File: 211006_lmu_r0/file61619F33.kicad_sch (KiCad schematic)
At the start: 46 parts, among them J5 Conn_01x03, J6 Conn_01x03, J7 Conn_01x02, Q1 CZT5551, U3 LTC6811HG-2#PBF

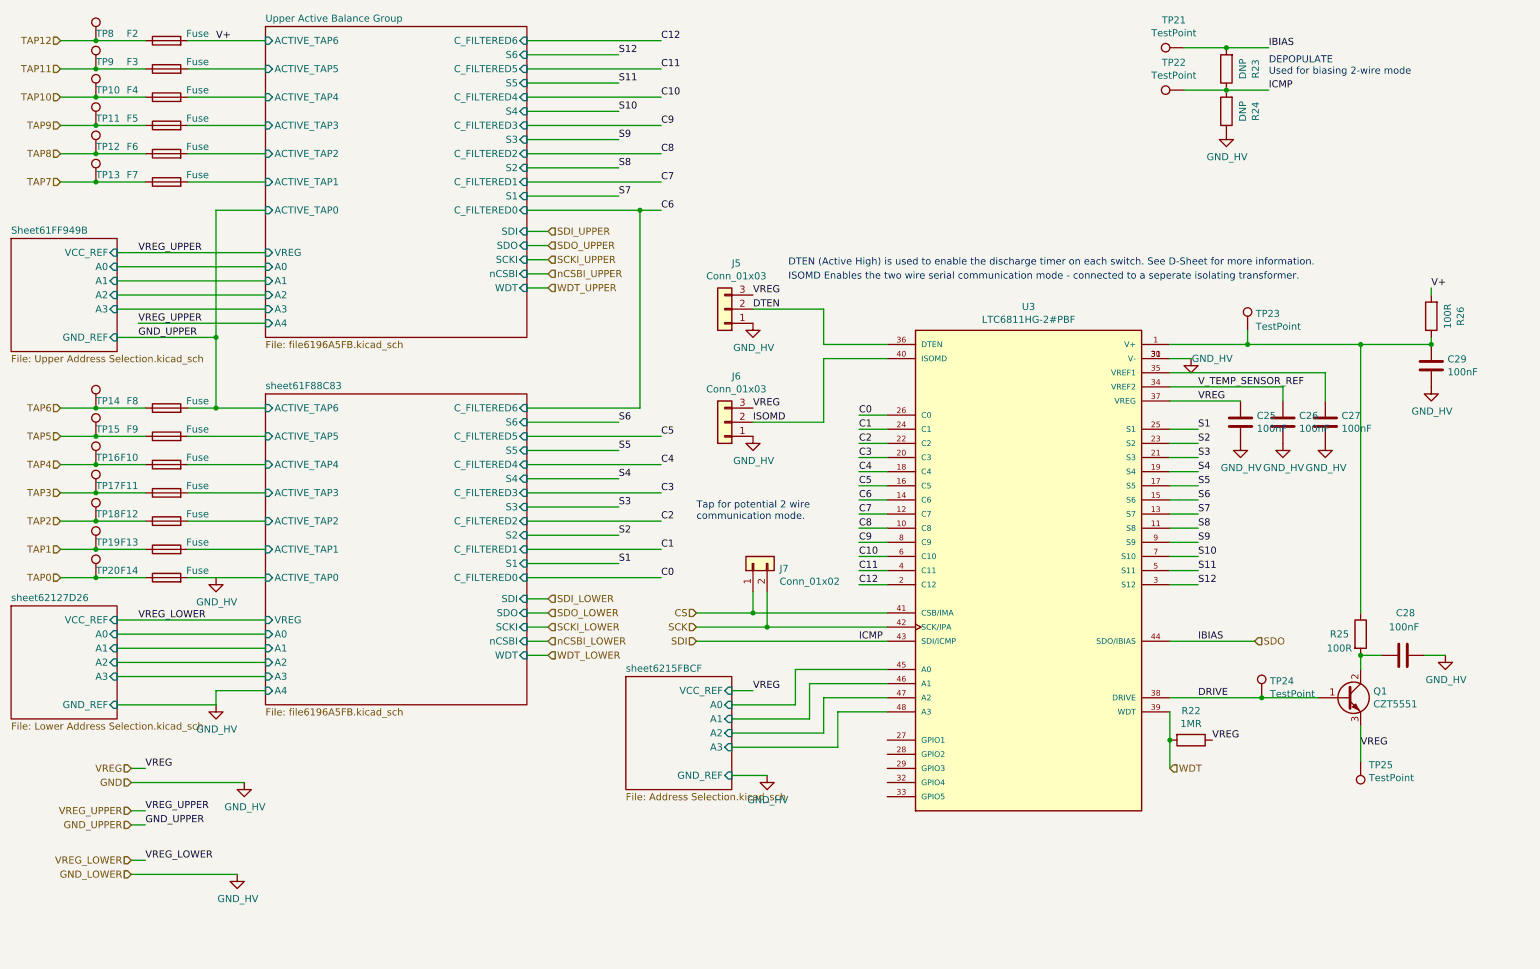
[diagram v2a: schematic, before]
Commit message: fixed footprints for headers, started planning out zones
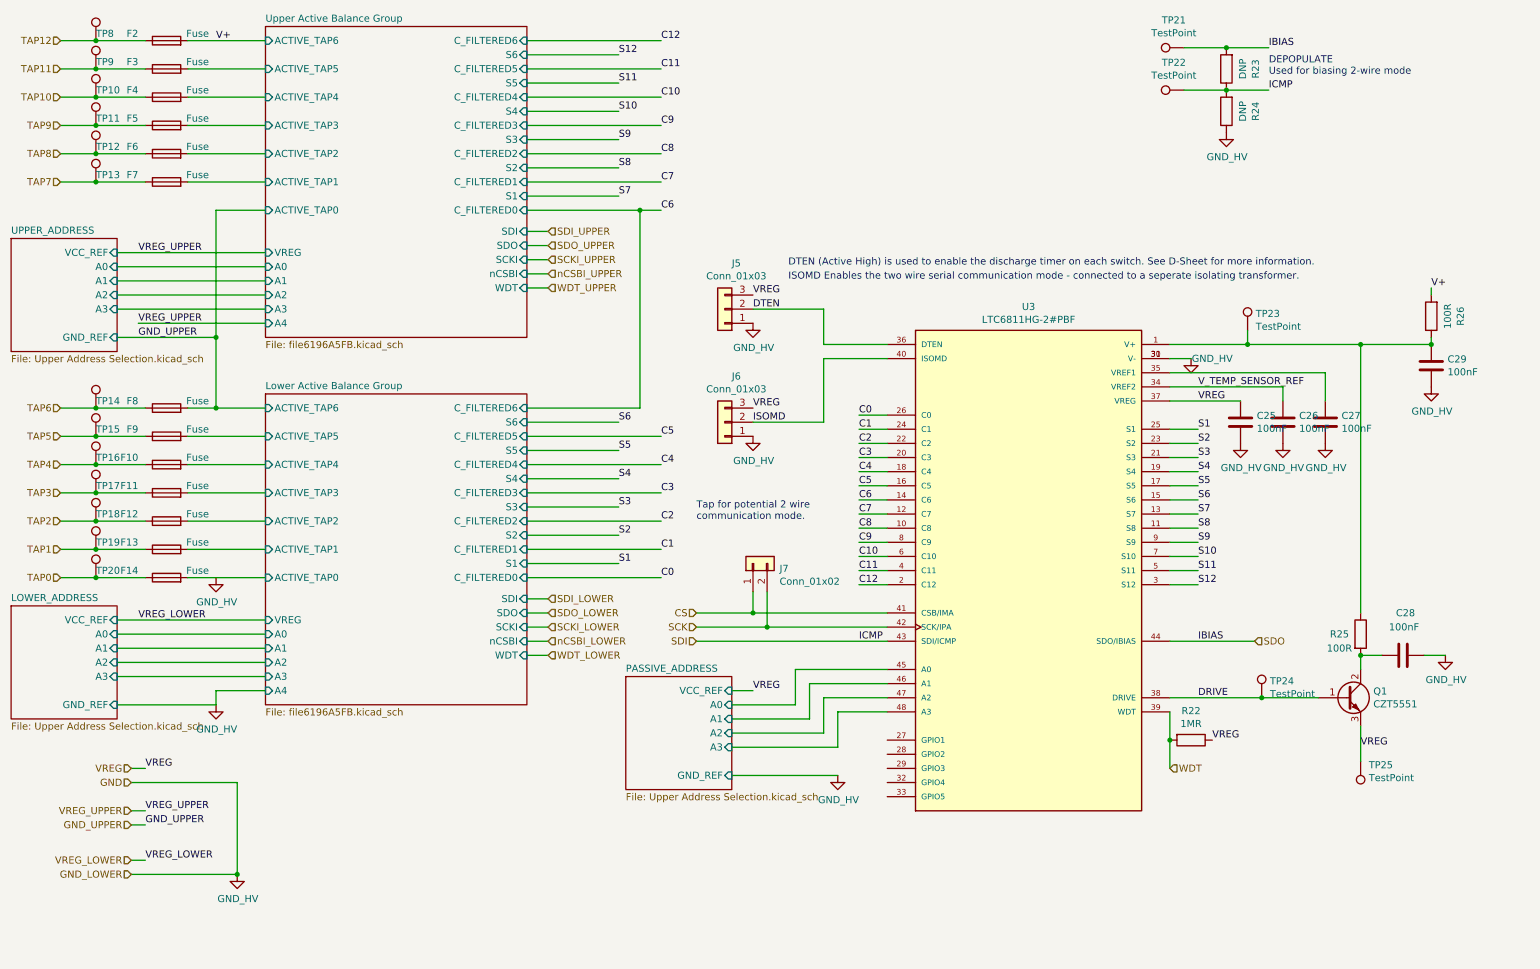
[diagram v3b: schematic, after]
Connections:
- net GND renamed GND_HV
- net sheet6215FBCF/A0 renamed PASSIVE_ADDRESS/A0
- net sheet6215FBCF/A1 renamed PASSIVE_ADDRESS/A1
- net sheet6215FBCF/A2 renamed PASSIVE_ADDRESS/A2
- net sheet6215FBCF/A3 renamed PASSIVE_ADDRESS/A3
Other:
- sheet Sheet61FF949B renamed UPPER_ADDRESS
- sheet sheet61F88C83 renamed Lower Active Balance Group
- removed sheet sheet62127D26
- removed sheet sheet6215FBCF
- added sheet LOWER_ADDRESS (Upper Address Selection.kicad_sch)
- added sheet PASSIVE_ADDRESS (Upper Address Selection.kicad_sch)
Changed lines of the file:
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@@
   (junction (at 33.02 29.21) (diameter 0) (color 0 0 0 0)
   )
+  (junction (at 58.42 173.99) (diameter 0) (color 0 0 0 0)
+  )
   (junction (at 33.02 44.45) (diameter 0) (color 0 0 0 0)
   )
@@
     (stroke (width 0) (type default) (color 0 0 0 0))
   )
+  (wire (pts (xy 58.42 157.48) (xy 58.42 173.99))
+    (stroke (width 0) (type default) (color 0 0 0 0))
+  )
   (wire (pts (xy 41.91 44.45) (xy 33.02 44.45))
     (stroke (width 0) (type default) (color 0 0 0 0))
@@
     (stroke (width 0) (type default) (color 0 0 0 0))
   )
-  (wire (pts (xy 39.37 157.48) (xy 59.69 157.48))
+  (wire (pts (xy 39.37 157.48) (xy 58.42 157.48))
     (stroke (width 0) (type default) (color 0 0 0 0))
   )
@@
     (stroke (width 0) (type default) (color 0 0 0 0))
   )
-  (wire (pts (xy 147.32 156.21) (xy 153.67 156.21))
+  (wire (pts (xy 147.32 156.21) (xy 166.37 156.21))
     (stroke (width 0) (type default) (color 0 0 0 0))
   )
@@
     (pin "2")
   )
-  (symbol (lib_id "gnd_hv:GND_HV") (at 54.61 120.65 0) (unit 1)
+  (symbol (lib_name "GND_HV_11") (lib_id "gnd_hv:GND_HV") (at 54.61 120.65 0) (unit 1)
     (in_bom yes) (on_board yes)
     (property "Reference" "#PWR040" (id 0) (at 54.61 127 0)
@@
     (pin "3")
   )
-  (symbol (lib_id "gnd_hv:GND_HV") (at 273.05 86.36 0) (unit 1)
+  (symbol (lib_name "GND_HV_1") (lib_id "gnd_hv:GND_HV") (at 273.05 86.36 0) (unit 1)
     (in_bom yes) (on_board yes)
     (property "Reference" "#PWR052" (id 0) (at 273.05 92.71 0)
@@
     (pin "2")
   )
-  (symbol (lib_id "gnd_hv:GND_HV") (at 275.59 134.62 0) (unit 1)
+  (symbol (lib_name "GND_HV_10") (lib_id "gnd_hv:GND_HV") (at 275.59 134.62 0) (unit 1)
     (in_bom yes) (on_board yes)
     (property "Reference" "#PWR053" (id 0) (at 275.59 140.97 0)
@@
     (pin "2")
   )
-  (symbol (lib_id "gnd_hv:GND_HV") (at 238.76 96.52 0) (unit 1)
+  (symbol (lib_name "GND_HV_4") (lib_id "gnd_hv:GND_HV") (at 238.76 96.52 0) (unit 1)
     (in_bom yes) (on_board yes)
     (property "Reference" "#PWR049" (id 0) (at 238.76 102.87 0)
@@
     (pin "2")
   )
-  (symbol (lib_id "gnd_hv:GND_HV") (at 246.38 96.52 0) (unit 1)
+  (symbol (lib_name "GND_HV_3") (lib_id "gnd_hv:GND_HV") (at 246.38 96.52 0) (unit 1)
     (in_bom yes) (on_board yes)
     (property "Reference" "#PWR050" (id 0) (at 246.38 102.87 0)
@@
     (pin "2")
   )
-  (symbol (lib_id "gnd_hv:GND_HV") (at 254 96.52 0) (unit 1)
+  (symbol (lib_name "GND_HV_2") (lib_id "gnd_hv:GND_HV") (at 254 96.52 0) (unit 1)
     (in_bom yes) (on_board yes)
     (property "Reference" "#PWR051" (id 0) (at 254 102.87 0)
@@
     (pin "1")
   )
-  (symbol (lib_id "gnd_hv:GND_HV") (at 229.87 81.28 0) (unit 1)
+  (symbol (lib_name "GND_HV_5") (lib_id "gnd_hv:GND_HV") (at 229.87 81.28 0) (unit 1)
     (in_bom yes) (on_board yes)
     (property "Reference" "#PWR047" (id 0) (at 229.87 87.63 0)
@@
     (pin "1")
   )
-  (symbol (lib_id "gnd_hv:GND_HV") (at 151.13 74.93 0) (unit 1)
+  (symbol (lib_name "GND_HV_6") (lib_id "gnd_hv:GND_HV") (at 151.13 74.93 0) (unit 1)
     (in_bom yes) (on_board yes)
     (property "Reference" "#PWR044" (id 0) (at 151.13 81.28 0)
@@
     (pin "3")
   )
-  (symbol (lib_id "gnd_hv:GND_HV") (at 151.13 95.25 0) (unit 1)
+  (symbol (lib_name "GND_HV_7") (lib_id "gnd_hv:GND_HV") (at 151.13 95.25 0) (unit 1)
     (in_bom yes) (on_board yes)
     (property "Reference" "#PWR045" (id 0) (at 151.13 101.6 0)
@@
     (pin "2")
   )
-  (symbol (lib_id "gnd_hv:GND_HV") (at 236.22 40.64 0) (unit 1)
+  (symbol (lib_name "GND_HV_8") (lib_id "gnd_hv:GND_HV") (at 236.22 40.64 0) (unit 1)
     (in_bom yes) (on_board yes)
     (property "Reference" "#PWR048" (id 0) (at 236.22 46.99 0)
@@
     (pin "1")
   )
-  (symbol (lib_id "gnd_hv:GND_HV") (at 153.67 156.21 0) (unit 1)
-    (in_bom yes) (on_board yes)
-    (property "Reference" "#PWR046" (id 0) (at 153.67 162.56 0)
-      (effects (font (size 1.27 1.27)) hide)
-    )
-    (property "Value" "GND_HV" (id 1) (at 153.797 160.6042 0))
-    (property "Footprint" "" (id 2) (at 153.67 156.21 0)
-      (effects (font (size 1.27 1.27)) hide)
-    )
-    (property "Datasheet" "" (id 3) (at 153.67 156.21 0)
-      (effects (font (size 1.27 1.27)) hide)
-    )
-    (pin "1")
-  )
-  (symbol (lib_id "gnd_hv:GND_HV") (at 58.42 173.99 0) (unit 1)
+  (symbol (lib_name "GND_HV_9") (lib_id "gnd_hv:GND_HV") (at 166.37 156.21 0) (unit 1)
+    (in_bom yes) (on_board yes)
+    (property "Reference" "#PWR046" (id 0) (at 166.37 162.56 0)
+      (effects (font (size 1.27 1.27)) hide)
+    )
+    (property "Value" "GND_HV" (id 1) (at 166.497 160.6042 0))
+    (property "Footprint" "" (id 2) (at 166.37 156.21 0)
+      (effects (font (size 1.27 1.27)) hide)
+    )
+    (property "Datasheet" "" (id 3) (at 166.37 156.21 0)
+      (effects (font (size 1.27 1.27)) hide)
+    )
+    (pin "1")
+  )
+  (symbol (lib_name "GND_HV_12") (lib_id "gnd_hv:GND_HV") (at 58.42 173.99 0) (unit 1)
     (in_bom yes) (on_board yes)
     (property "Reference" "#PWR042" (id 0) (at 58.42 180.34 0)
@@
     )
     (property "Datasheet" "" (id 3) (at 58.42 173.99 0)
-      (effects (font (size 1.27 1.27)) hide)
-    )
-    (pin "1")
-  )
-  (symbol (lib_id "gnd_hv:GND_HV") (at 59.69 157.48 0) (unit 1)
-    (in_bom yes) (on_board yes)
-    (property "Reference" "#PWR043" (id 0) (at 59.69 163.83 0)
-      (effects (font (size 1.27 1.27)) hide)
-    )
-    (property "Value" "GND_HV" (id 1) (at 59.817 161.8742 0))
-    (property "Footprint" "" (id 2) (at 59.69 157.48 0)
-      (effects (font (size 1.27 1.27)) hide)
-    )
-    (property "Datasheet" "" (id 3) (at 59.69 157.48 0)
       (effects (font (size 1.27 1.27)) hide)
     )
@@
     (stroke (width 0) (type solid) (color 0 0 0 0))
     (fill (color 0 0 0 0.0000))
-    (property "Sheet name" "sheet61F88C83" (id 0) (at 63.5 86.9184 0)
+    (property "Sheet name" "Lower Active Balance Group" (id 0) (at 63.5 86.9184 0)
       (effects (font (size 1.27 1.27)) (justify left bottom))
     )
@@
     (stroke (width 0) (type solid) (color 0 0 0 0))
     (fill (color 0 0 0 0.0000))
-    (property "Sheet name" "Sheet61FF949B" (id 0) (at 17.78 58.9784 0)
+    (property "Sheet name" "UPPER_ADDRESS" (id 0) (at 17.78 58.9784 0)
       (effects (font (size 1.27 1.27)) (justify left bottom))
     )
@@
     )
     (pin "A3" input (at 36.83 72.39 0)
+      (effects (font (size 1.27 1.27)) (justify right))
+    )
+  )
+  (sheet (at 128.27 138.43) (size 19.05 20.32) (fields_autoplaced)
+    (stroke (width 0) (type solid) (color 0 0 0 0))
+    (fill (color 0 0 0 0.0000))
+    (property "Sheet name" "PASSIVE_ADDRESS" (id 0) (at 128.27 137.7184 0)
+      (effects (font (size 1.27 1.27)) (justify left bottom))
+    )
+    (property "Sheet file" "Upper Address Selection.kicad_sch" (id 1) (at 128.27 159.3346 0)
+      (effects (font (size 1.27 1.27)) (justify left top))
+    )
+    (pin "GND_REF" input (at 147.32 156.21 0)
+      (effects (font (size 1.27 1.27)) (justify right))
+    )
+    (pin "VCC_REF" input (at 147.32 140.97 0)
+      (effects (font (size 1.27 1.27)) (justify right))
+    )
+    (pin "A0" input (at 147.32 143.51 0)
+      (effects (font (size 1.27 1.27)) (justify right))
+    )
+    (pin "A1" input (at 147.32 146.05 0)
+      (effects (font (size 1.27 1.27)) (justify right))
+    )
+    (pin "A2" input (at 147.32 148.59 0)
+      (effects (font (size 1.27 1.27)) (justify right))
+    )
+    (pin "A3" input (at 147.32 151.13 0)
       (effects (font (size 1.27 1.27)) (justify right))
     )
@@
     (stroke (width 0) (type solid) (color 0 0 0 0))
     (fill (color 0 0 0 0.0000))
-    (property "Sheet name" "sheet62127D26" (id 0) (at 17.78 125.0184 0)
+    (property "Sheet name" "LOWER_ADDRESS" (id 0) (at 17.78 125.0184 0)
       (effects (font (size 1.27 1.27)) (justify left bottom))
     )
-    (property "Sheet file" "Lower Address Selection.kicad_sch" (id 1) (at 17.78 146.6346 0)
+    (property "Sheet file" "Upper Address Selection.kicad_sch" (id 1) (at 17.78 146.6346 0)
       (effects (font (size 1.27 1.27)) (justify left top))
     )
@@
       (effects (font (size 1.27 1.27)) (justify right))
     )
-  )
-  (sheet (at 128.27 138.43) (size 19.05 20.32) (fields_autoplaced)
-    (stroke (width 0) (type solid) (color 0 0 0 0))
-    (fill (color 0 0 0 0.0000))
-    (property "Sheet name" "sheet6215FBCF" (id 0) (at 128.27 137.7184 0)
-      (effects (font (size 1.27 1.27)) (justify left bottom))
-    )
-    (property "Sheet file" "Address Selection.kicad_sch" (id 1) (at 128.27 159.3346 0)
-      (effects (font (size 1.27 1.27)) (justify left top))
-    )
-    (pin "GND_REF" input (at 147.32 156.21 0)
-      (effects (font (size 1.27 1.27)) (justify right))
-    )
-    (pin "VCC_REF" input (at 147.32 140.97 0)
-      (effects (font (size 1.27 1.27)) (justify right))
-    )
-    (pin "A0" input (at 147.32 143.51 0)
-      (effects (font (size 1.27 1.27)) (justify right))
-    )
-    (pin "A1" input (at 147.32 146.05 0)
-      (effects (font (size 1.27 1.27)) (justify right))
-    )
-    (pin "A2" input (at 147.32 148.59 0)
-      (effects (font (size 1.27 1.27)) (justify right))
-    )
-    (pin "A3" input (at 147.32 151.13 0)
-      (effects (font (size 1.27 1.27)) (justify right))
-    )
